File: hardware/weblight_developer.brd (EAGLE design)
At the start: 31.8 x 12 mm, 14 parts, among them U1 ATtiny85-20SU

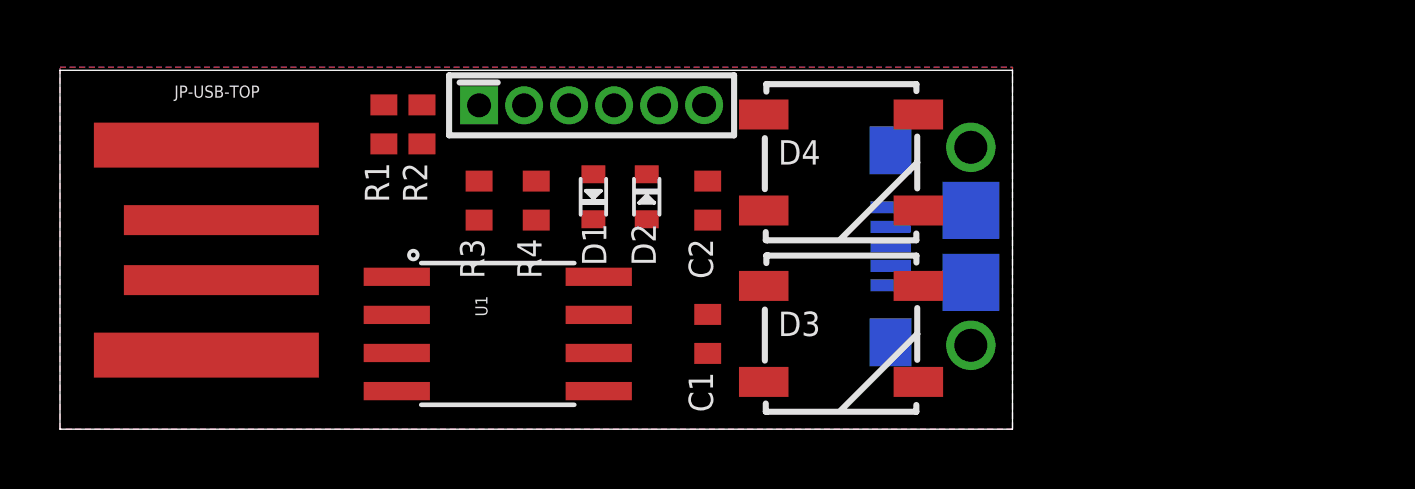
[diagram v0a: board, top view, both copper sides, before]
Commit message: Developer board changes.
Convert every 0402 SMD to 0805.
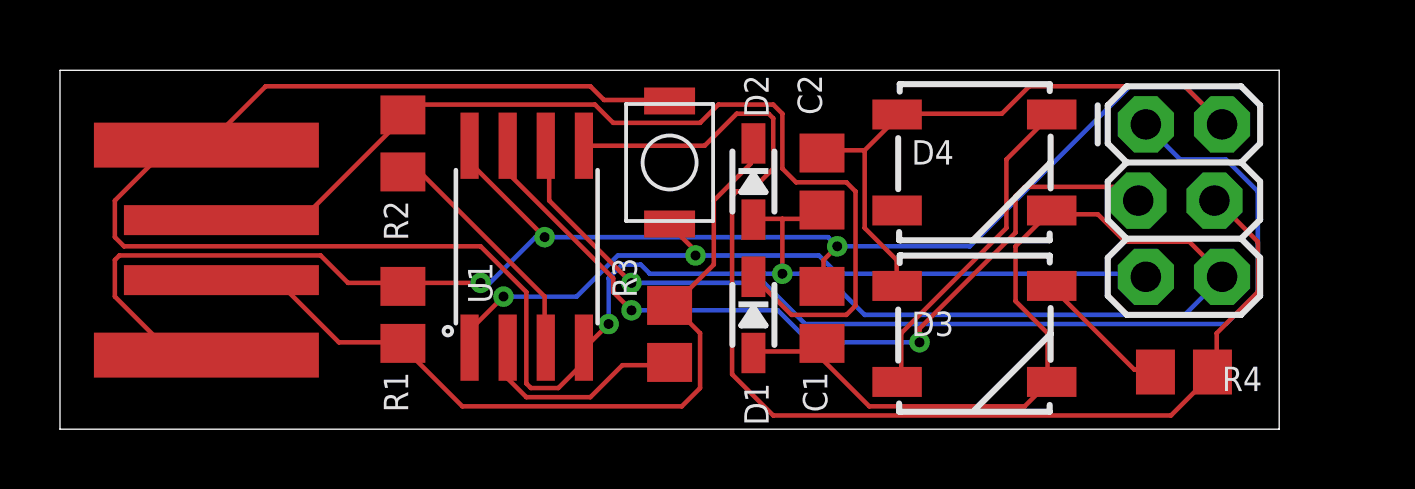
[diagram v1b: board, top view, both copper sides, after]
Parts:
- removed JP-ISP: AVR_MINI_PROGSMD, SparkFun-Connectors:AVR_MINI_PROG
- removed JP-USB-MICRO: (no value), MF_Connectors:MICROUSB-RIGHT
- added JP1: AVR_SPI_PRG_62X3_LOCK, SparkFun-Connectors:2X3_LOCK
- added SW_RESET: BUTTON_TD-85XU, weblight:BUTTON_TD-85XU
- C1, C2: device rcl:C0402 -> rcl:C0805
- D1, D2: device microbuilder:SOD-523 -> microbuilder:SOD-323
- R1, R2, R3, R4: device rcl:R0402 -> rcl:R0805
- moved R4 22.3 mm to (37.5, 1.91), turned to 0 degrees
- moved R3 7.75 mm to (20.3, 3.17)
- moved D1 6.63 mm to (23.1, 3.81), turned to 270 degrees
- moved R1 6.38 mm to (11.4, 3.81)
- moved D3 4.45 mm to (30.5, 3.17)
- moved D4 4.45 mm to (30.5, 8.89)
- moved C1 3.86 mm to (25.4, 3.81)
- moved C2 3.86 mm to (25.4, 8.26)
- moved D2 3.59 mm to (23.1, 8.26), turned to 270 degrees
- moved U1 3.07 mm to (15.6, 6.10), turned to 0 degrees
- moved R2 0.90 mm to (11.4, 9.53)
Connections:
- net N$1 renamed DIN_1
- removed net MOSI/DIN: JP-ISP.4, R4.2, U1.5
- removed net SLD: JP-USB-MICRO.S1, JP-USB-MICRO.S2, JP-USB-MICRO.S3, JP-USB-MICRO.S4, JP-USB-MICRO.S5, JP-USB-MICRO.S6
- new net MOSI/DIN_RAW: JP1.4, R4.2, U1.5
- net GND: now also JP1.6, SW_RESET.PAD2; no longer JP-ISP.2, JP-USB-MICRO.5
- net MISO: now also JP1.1; no longer JP-ISP.6
- net RESET: now also JP1.5, SW_RESET.PAD1; no longer JP-ISP.3
- net SCK: now also JP1.3; no longer JP-ISP.5
- net USB_D_MINUS: now also R3.1; no longer R3.2
- net USB_D_MINUS_RAW: now also D2.C, R1.2, R3.2; no longer D2.K, JP-USB-MICRO.2, R1.1, R3.1
- net USB_D_PLUS_RAW: now also D1.C; no longer D1.K, JP-USB-MICRO.3
- net VCC: now also JP1.2, R1.1; no longer JP-ISP.1, JP-USB-MICRO.1, R1.2
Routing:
- net GND: track 0.00 -> 95.8 mm, vias 0 -> 2
- net VCC: track 0.00 -> 71.6 mm, vias 0 -> 3
- net MOSI/DIN_RAW: track 0.00 -> 40.4 mm
- net MISO: track 0.00 -> 35.7 mm, vias 0 -> 1
- net USB_D_PLUS_RAW: track 0.00 -> 33.5 mm
- net SCK: track 0.00 -> 27.9 mm, vias 0 -> 2
- net USB_D_MINUS_RAW: track 0.00 -> 27.8 mm
- net RESET: track 0.00 -> 25.9 mm, vias 0 -> 2
- net DIN_2: track 0.00 -> 11.1 mm
- net USB_D_PLUS: track 0.00 -> 8.19 mm
- net USB_D_MINUS: track 0.00 -> 7.17 mm
- net DIN_1: track 0.00 -> 4.66 mm
- removed copper zone on layer 1, net GND
- removed copper zone on layer 16, net GND
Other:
- board size 31.8 x 12 mm -> 40.6 x 12 mm
- board text added: "Version osh3"
- board text added: "github.com/sowbug/weblight"
- board text removed: "Version mf3"
- board text removed: "mike@sowbug.com"

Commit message: osh3 rc1
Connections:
- net USB_D_MINUS_RAW: now also R1.1; no longer R1.2
- net USB_D_PLUS: now also R2.1; no longer R2.2
- net USB_D_PLUS_RAW: now also R2.2; no longer R2.1
- net VCC: now also R1.2; no longer R1.1
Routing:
- net RESET: track 25.9 -> 62.3 mm, vias 2 -> 0
- net VCC: track 71.6 -> 56.9 mm
- net USB_D_PLUS_RAW: track 33.5 -> 21.4 mm
- net MOSI/DIN_RAW: track 40.4 -> 30.7 mm, vias 0 -> 1
- net MISO: track 35.7 -> 45.3 mm, vias 1 -> 0
- net USB_D_MINUS_RAW: track 27.8 -> 22.2 mm, vias 0 -> 2
- net SCK: track 27.9 -> 23.8 mm, vias 2 -> 1
- net GND: track 95.8 -> 93.3 mm, vias 2 -> 3
- net USB_D_PLUS: track 8.19 -> 9.73 mm, vias 0 -> 2
- net USB_D_MINUS: track 7.17 -> 6.65 mm
- added copper zone on layer 1, net GND
- added copper zone on layer 16, net GND

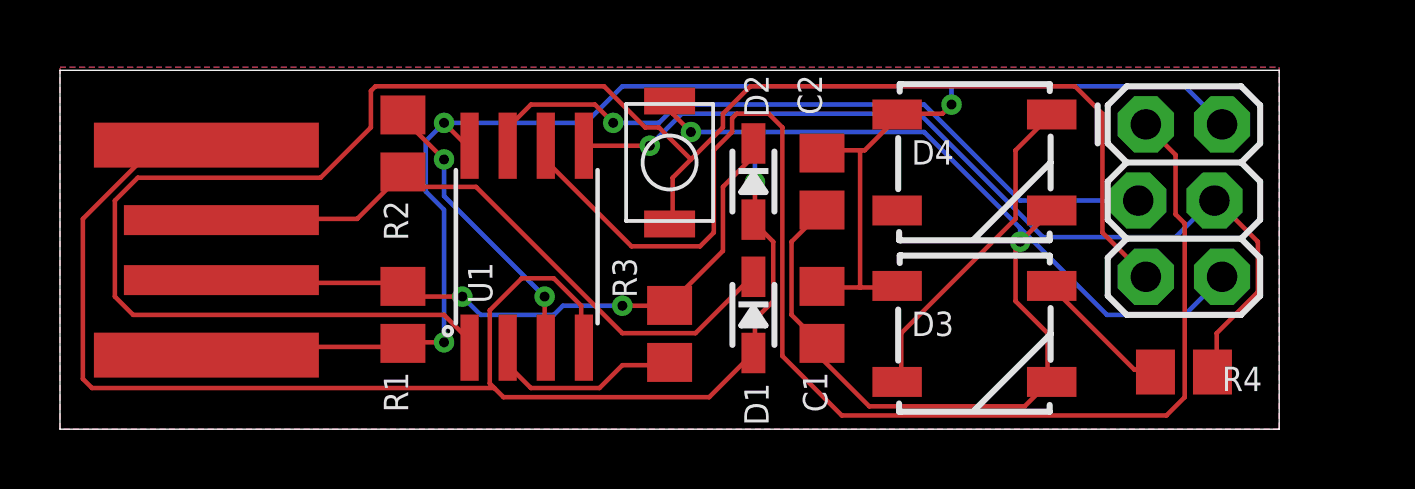
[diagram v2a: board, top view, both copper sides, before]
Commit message: Move developer board to APA102C
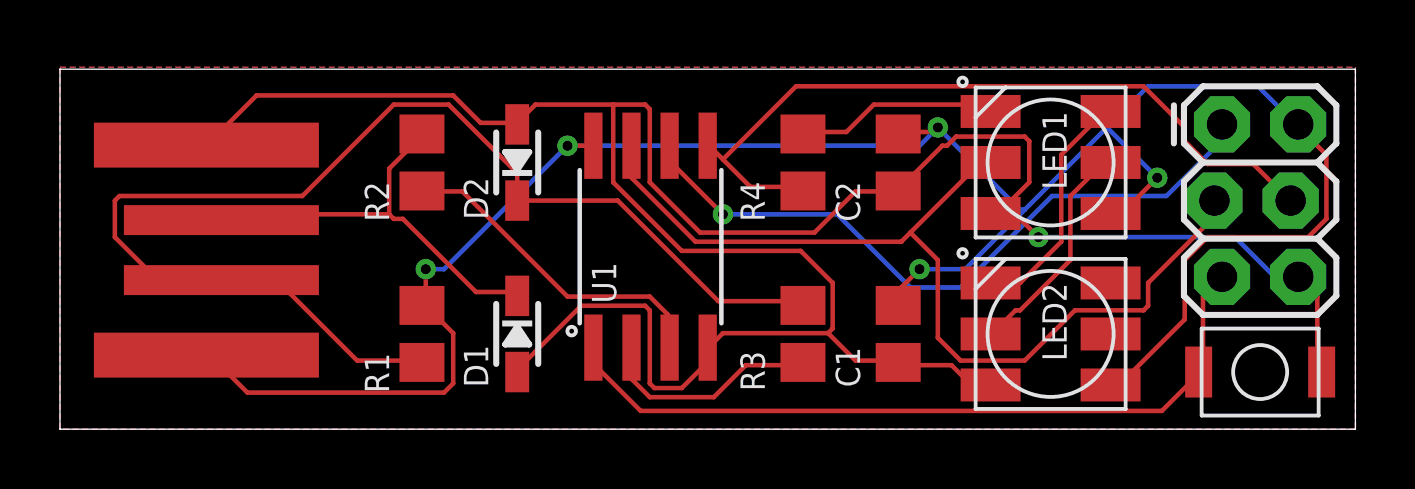
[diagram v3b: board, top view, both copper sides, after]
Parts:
- removed D3, D4: WS2812B, SparkFun-LED:WS2812B
- added LED1, LED2: APA102, weblight:APA102
- U1: value ATtiny85-20SU -> ATTiny85-20SU
- moved SW_RESET 20.9 mm to (40.0, 1.91), turned to 0 degrees
- moved R4 14.5 mm to (24.8, 8.89), turned to 90 degrees
- moved D1 7.90 mm to (15.2, 3.17)
- moved D2 7.90 mm to (15.2, 8.89), turned to 90 degrees
- moved R3 4.45 mm to (24.8, 3.17)
- moved U1 4.13 mm to (19.7, 6.10)
- moved C1 2.62 mm to (27.9, 3.17)
- moved C2 2.62 mm to (27.9, 8.89)
- moved JP1 2.54 mm to (38.7, 10.2)
- moved R1 0.90 mm to (12.1, 3.17)
- moved R2 0.90 mm to (12.1, 8.89)
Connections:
- removed net SCK: JP1.3, U1.7
- new net SCK_1: JP1.3, LED1.CI, U1.7
- new net SCK_2: LED1.CO, LED2.CI
- net DIN_1: now also LED1.DI, R4.2; no longer D3.4, R4.1
- net DIN_2: now also LED1.DO, LED2.DI; no longer D3.2, D4.4
- net GND: now also LED1.GND, LED2.GND; no longer D3.3, D4.3
- net MOSI/DIN_RAW: now also R4.1; no longer R4.2
- net USB_D_MINUS_RAW: now also R1.2; no longer R1.1
- net USB_D_PLUS: now also R2.2; no longer R2.1
- net USB_D_PLUS_RAW: now also R2.1; no longer R2.2
- net VCC: now also LED1.VCC, LED2.VCC, R1.1; no longer D3.1, D4.1, R1.2
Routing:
- net RESET: track 62.3 -> 25.4 mm
- net SCK_1: track 0.00 -> 31.4 mm
- net SCK: track 23.8 -> 0.00 mm, vias 1 -> 0
- net MISO: track 45.3 -> 23.3 mm, vias 0 -> 1
- net USB_D_MINUS_RAW: track 22.2 -> 40.8 mm, vias 2 -> 0
- net VCC: track 56.9 -> 74.3 mm, vias 3 -> 5
- net GND: track 93.3 -> 85.5 mm, vias 3 -> 1
- net SCK_2: track 0.00 -> 7.69 mm
- net USB_D_PLUS_RAW: track 21.4 -> 14.3 mm
- net MOSI/DIN_RAW: track 30.7 -> 25.6 mm, vias 1 -> 0
- net DIN_2: track 11.1 -> 8.12 mm
- net DIN_1: track 4.66 -> 6.75 mm
- net USB_D_PLUS: track 9.73 -> 11.0 mm, vias 2 -> 0
- net USB_D_MINUS: track 6.65 -> 7.49 mm
- added copper zone on layer 16, net N$1
- added copper zone on layer 1, net N$2
- removed copper zone on layer 1, net GND
- removed copper zone on layer 16, net GND
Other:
- board size 40.6 x 12 mm -> 43.2 x 12 mm
- board text added: "Version osh4"
- board text removed: "Version osh3"
